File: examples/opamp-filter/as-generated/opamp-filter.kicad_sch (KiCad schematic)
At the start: 17 parts, among them J1 IN, J2 5V, J3 OUT, U1 MCP6001R, U2 MCP6001R

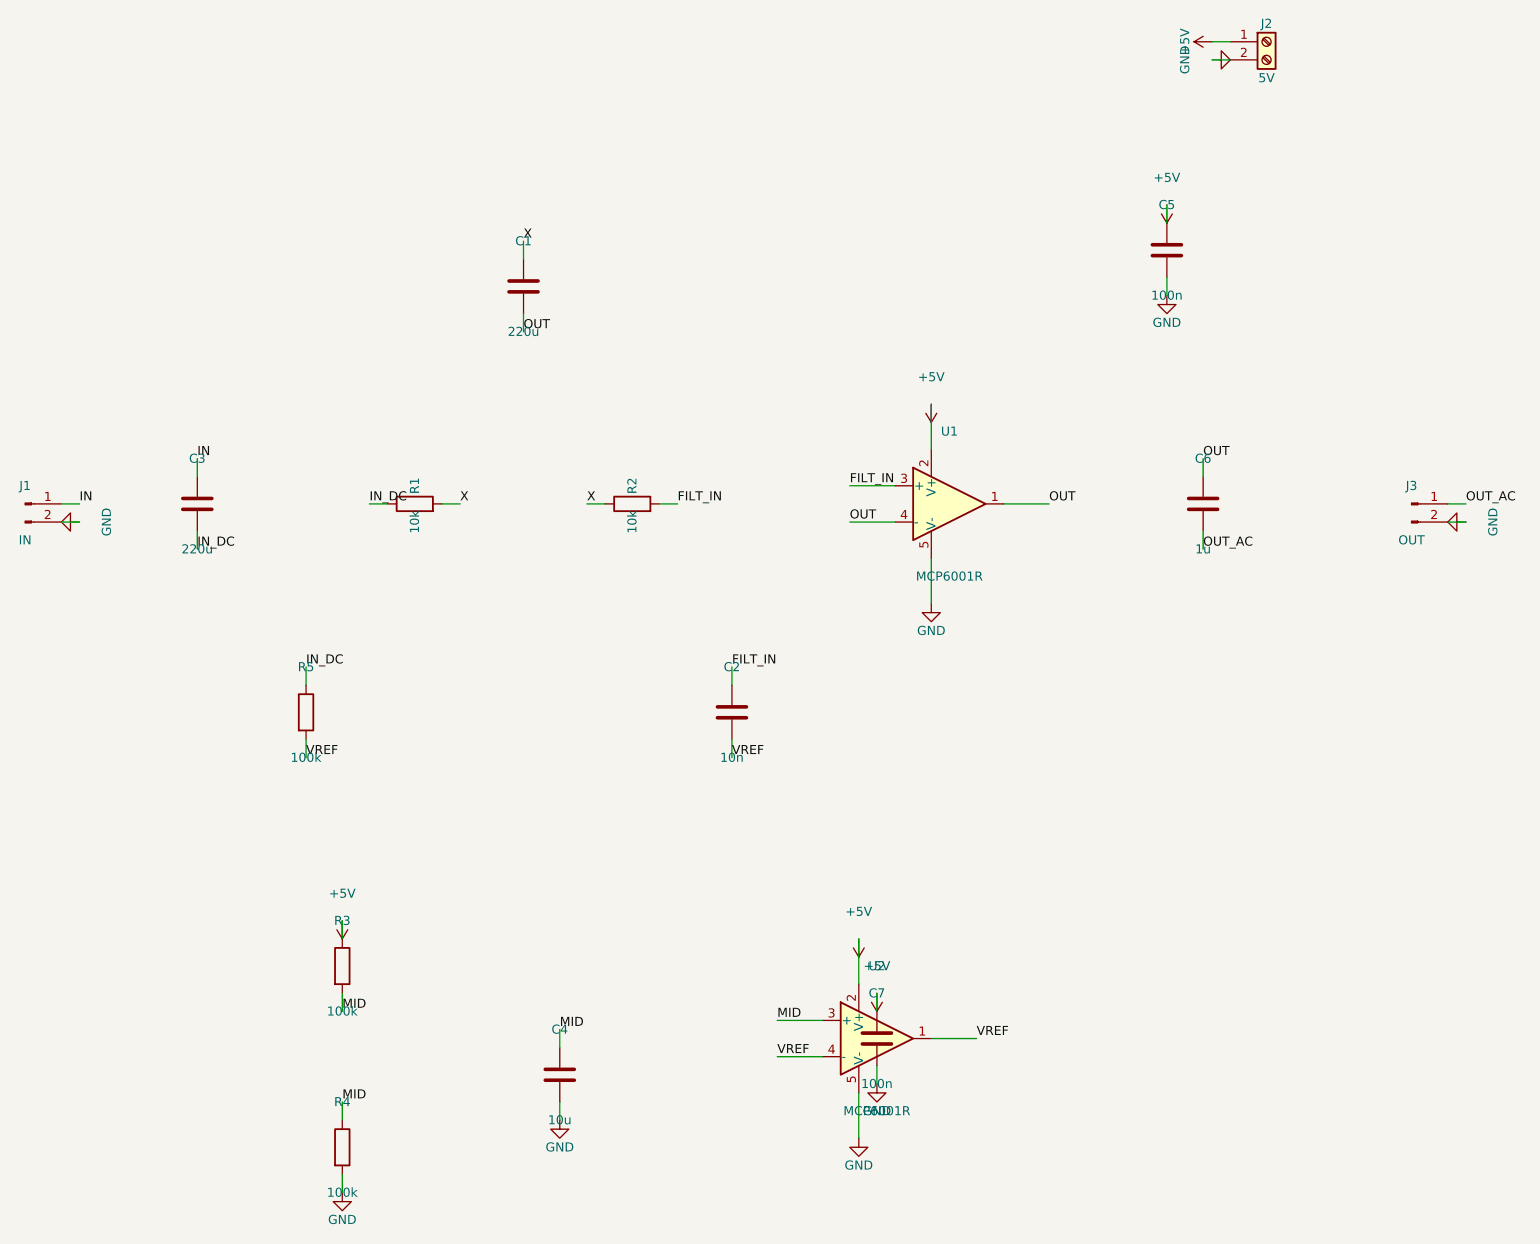
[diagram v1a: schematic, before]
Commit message: Read the five as an engineer would, and make the toolkit act on it
examples/REVIEW.md is the pass: the five designs read for circuit theory,
layout physics and readability, every finding dispatched to one of four
places - a rule, a fix, a reasoned waiver, or named as open. The headline
result: every reviewed/ project now PASSES its own gate, every as-generated/
still fails it, and every waiver is an engineering argument a reviewer can
disagree with.

Four new rules, each calibrated against KiCad's 18 human-drawn demo projects:

* readability.label_only - the sheet connects by name, not by wire; the
  single most recognisable mark of a generated schematic. 0 findings on the
  human corpus, 71-100% on ours.
* analog.no_dc_path - a net of only capacitors and connectors has nothing
  setting its DC level. Found a real fault: the op-amp filter's AC-coupled
  output floated. 0 findings on the corpus.
* route.detour - routed copper against the MST of the net's pads; the scenic
  tour an autorouter takes. 8 human boards fired at 2.5x, 0 at the shipped 4x.
* route.return_path - signal running over cuts in the other layer's ground
  fill, computed from the difference between a zone's outline and its fill,
  which the parser now keeps. Fires on 4 real demo boards, because real
  two-layer boards genuinely have the disease.

Three rules re-judged on evidence instead of names:

* analog.missing_decoupling reads pin electrical types: only power_in pins
  ask for a capacitor, and a net an output pin drives is never asked - a cap
  on an op-amp output is somebody's control loop. Retires the VBUS/VREF
  false positives without a single waiver.
* track.thin_power measures the longest contiguous narrow run against a
  power_neck_mm allowance. Pad entries and fine-pitch escapes pass; thin
  trunks still fail. 9 demo boards fired before, 0 after - all nine were necks.
* net.single_pin honours no-connect flags: a flagged pin is a decision.

And the designs themselves got the fixes the pa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
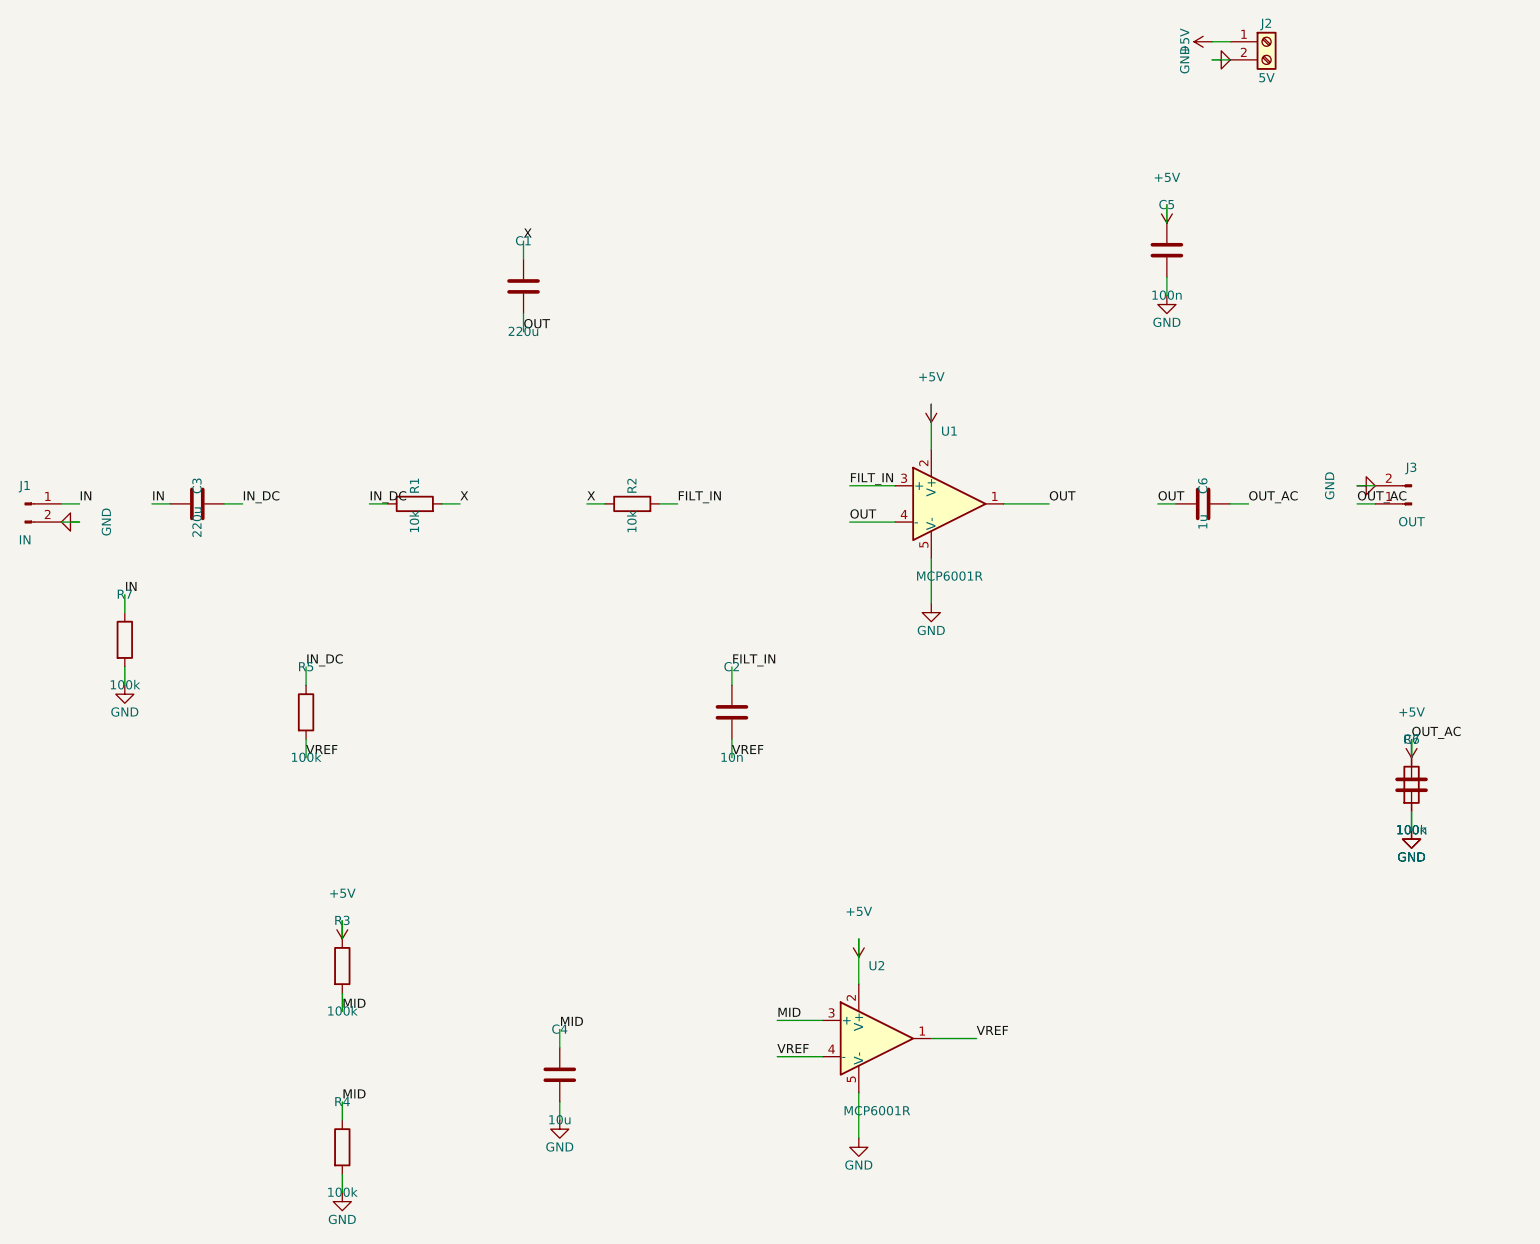
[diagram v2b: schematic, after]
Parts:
- added R6, R7: 100k, Resistor_SMD:R_0805_2012Metric, symbol Device:R
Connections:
- net OUT_AC is gone; now on net +5V: C6.2, J3.1 (Pin_1)
- net +5V: now also R6.1
- net GND: now also R6.2, R7.2
- net IN: now also R7.1
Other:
- moved on the sheet: C3, C6, C7, J3
